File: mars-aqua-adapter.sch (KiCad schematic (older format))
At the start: 40 parts, among them J1 Conn_01x03, J2 Conn_01x03, J3 Conn_01x04, J4 Conn_01x04, J5 Conn_01x03, J6 Conn_01x03, Q2 Q_PNP_BEC, U1 LM358, U2 LM393

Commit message: Final Layout
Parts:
- C1, C4: footprint Capacitor_SMD:C_1206_3216Metric_Pad1.42x1.75mm_HandSolder -> Capacitor_SMD:C_0805_2012Metric
- C2, C3: value 0.1uF -> 4.7uF; footprint Capacitor_SMD:C_1206_3216Metric_Pad1.42x1.75mm_HandSolder -> Capacitor_SMD:C_0805_2012Metric
- gave numbers to parts that had none: 1
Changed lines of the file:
@@
 P 3500 2850
 F 0 "C2" H 3592 2896 50  0000 L CNN
-F 1 "0.1uF" H 3592 2805 50  0000 L CNN
-F 2 "Capacitor_SMD:C_1206_3216Metric_Pad1.42x1.75mm_HandSolder" H 3500 2850 50  0001 C CNN
+F 1 "4.7uF" H 3592 2805 50  0000 L CNN
+F 2 "Capacitor_SMD:C_0805_2012Metric" H 3500 2850 50  0001 C CNN
 F 3 "~" H 3500 2850 50  0001 C CNN
 	1    3500 2850
@@
 F 0 "C4" H 6942 1246 50  0000 L CNN
 F 1 "0.1uF" H 6942 1155 50  0000 L CNN
-F 2 "Capacitor_SMD:C_1206_3216Metric_Pad1.42x1.75mm_HandSolder" H 6850 1200 50  0001 C CNN
+F 2 "Capacitor_SMD:C_0805_2012Metric" H 6850 1200 50  0001 C CNN
 F 3 "~" H 6850 1200 50  0001 C CNN
 	1    6850 1200
@@
 F 0 "C1" H 3792 1646 50  0000 L CNN
 F 1 "0.1uF" H 3792 1555 50  0000 L CNN
-F 2 "Capacitor_SMD:C_1206_3216Metric_Pad1.42x1.75mm_HandSolder" H 3700 1600 50  0001 C CNN
+F 2 "Capacitor_SMD:C_0805_2012Metric" H 3700 1600 50  0001 C CNN
 F 3 "~" H 3700 1600 50  0001 C CNN
 	1    3700 1600
@@
 P 3500 5150
 F 0 "C3" H 3592 5196 50  0000 L CNN
-F 1 "0.1uF" H 3592 5105 50  0000 L CNN
-F 2 "Capacitor_SMD:C_1206_3216Metric_Pad1.42x1.75mm_HandSolder" H 3500 5150 50  0001 C CNN
+F 1 "4.7uF" H 3592 5105 50  0000 L CNN
+F 2 "Capacitor_SMD:C_0805_2012Metric" H 3500 5150 50  0001 C CNN
 F 3 "~" H 3500 5150 50  0001 C CNN
 	1    3500 5150
@@
 $EndComp
 $Comp
-L Device:Q_PNP_BEC Q?
+L Device:Q_PNP_BEC Q1
 U 1 1 5C86EAA4
 P 8200 2600
-F 0 "Q?" H 8391 2554 50  0000 L CNN
+F 0 "Q1" H 8391 2554 50  0000 L CNN
 F 1 "Q_PNP_BEC" H 8391 2645 50  0000 L CNN
 F 2 "Package_TO_SOT_SMD:SOT-23" H 8400 2700 50  0001 C CNN

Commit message: Fix traces on comparator
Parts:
- R11, R13: value 30k -> 39k
- R12, R14: value 10k -> 20k
- VR1, VR2: value TRIMPOT-SMD-3MM-OPEN-1_10W-25% -> 10k
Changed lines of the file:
@@
 P 6000 2750
 F 0 "R12" H 6068 2796 50  0000 L CNN
-F 1 "10k" H 6068 2705 50  0000 L CNN
+F 1 "20k" H 6068 2705 50  0000 L CNN
 F 2 "Resistor_SMD:R_0603_1608Metric_Pad1.05x0.95mm_HandSolder" V 6040 2740 50  0001 C CNN
 F 3 "~" H 6000 2750 50  0001 C CNN
@@
 P 6000 2350
 F 0 "R11" H 6068 2396 50  0000 L CNN
-F 1 "30k" H 6068 2305 50  0000 L CNN
+F 1 "39k" H 6068 2305 50  0000 L CNN
 F 2 "Resistor_SMD:R_0603_1608Metric_Pad1.05x0.95mm_HandSolder" V 6040 2340 50  0001 C CNN
 F 3 "~" H 6000 2350 50  0001 C CNN
@@
 P 6000 1900
 F 0 "VR1" H 5933 1805 45  0000 R CNN
-F 1 "TRIMPOT-SMD-3MM-OPEN-1_10W-25%" H 5933 1889 45  0000 R CNN
+F 1 "10k" H 5933 1889 45  0000 R CNN
 F 2 "Resistors:TRIMPOT-SMD-3MM-OPEN" V 5850 1900 20  0001 C CNN
 F 3 "" H 6000 1900 60  0001 C CNN
@@
 P 6000 5050
 F 0 "R14" H 6068 5096 50  0000 L CNN
-F 1 "10k" H 6068 5005 50  0000 L CNN
+F 1 "20k" H 6068 5005 50  0000 L CNN
 F 2 "Resistor_SMD:R_0603_1608Metric_Pad1.05x0.95mm_HandSolder" V 6040 5040 50  0001 C CNN
 F 3 "~" H 6000 5050 50  0001 C CNN
@@
 P 6000 4650
 F 0 "R13" H 6068 4696 50  0000 L CNN
-F 1 "30k" H 6068 4605 50  0000 L CNN
+F 1 "39k" H 6068 4605 50  0000 L CNN
 F 2 "Resistor_SMD:R_0603_1608Metric_Pad1.05x0.95mm_HandSolder" V 6040 4640 50  0001 C CNN
 F 3 "~" H 6000 4650 50  0001 C CNN
@@
 P 6000 4200
 F 0 "VR2" H 5933 4105 45  0000 R CNN
-F 1 "TRIMPOT-SMD-3MM-OPEN-1_10W-25%" H 5933 4189 45  0000 R CNN
+F 1 "10k" H 5933 4189 45  0000 R CNN
 F 2 "Resistors:TRIMPOT-SMD-3MM-OPEN" V 5850 4200 20  0001 C CNN
 F 3 "" H 6000 4200 60  0001 C CNN

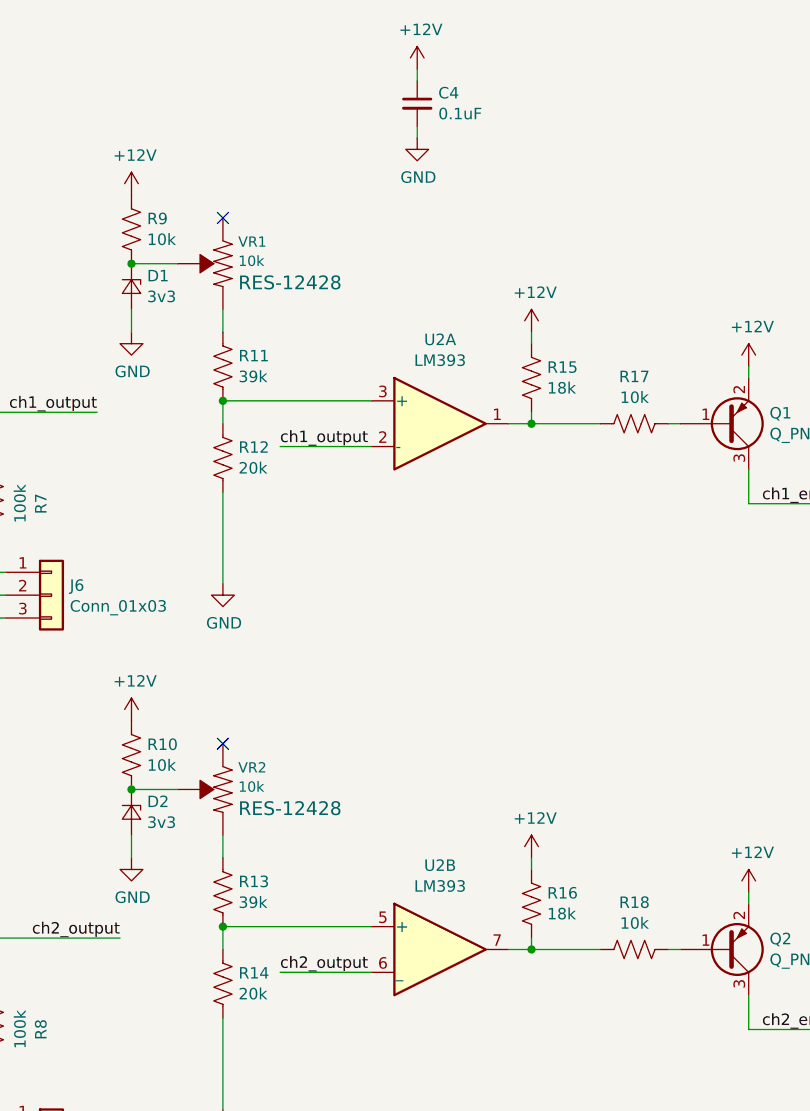
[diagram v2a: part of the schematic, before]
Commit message: Add hysteresis
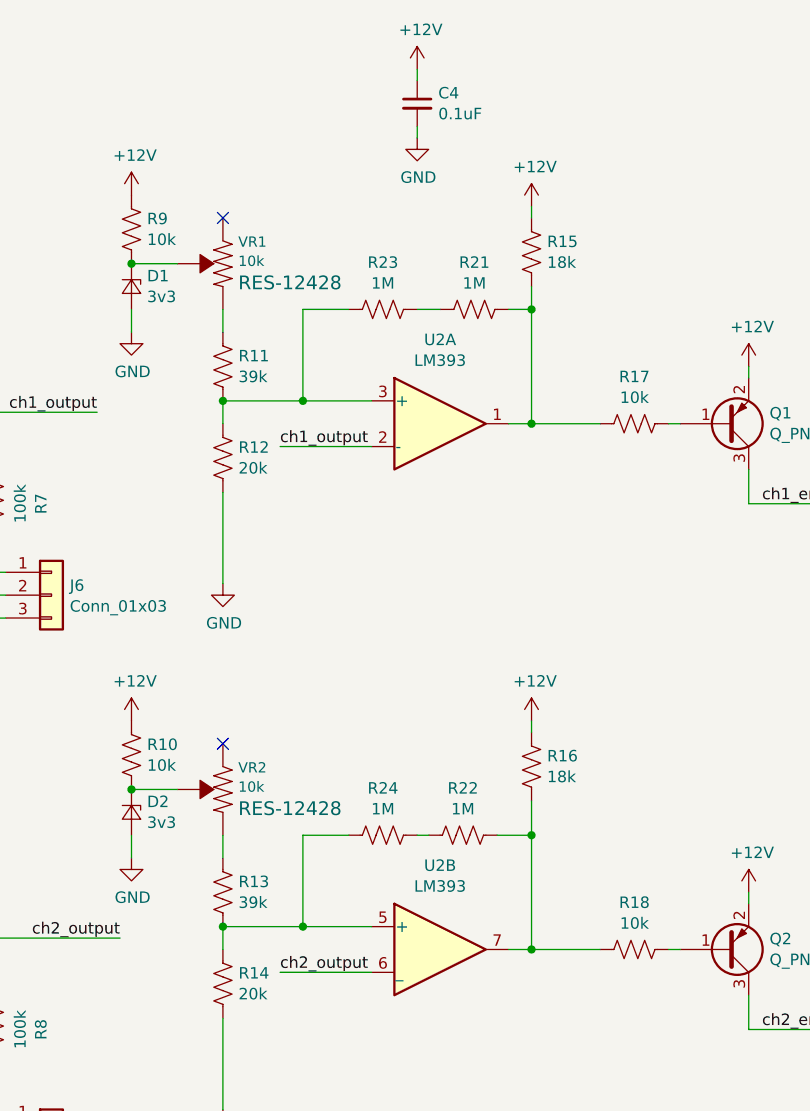
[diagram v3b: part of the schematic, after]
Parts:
- added R21, R22, R23, R24: 1M, Resistor_SMD:R_0603_1608Metric_Pad1.05x0.95mm_HandSolder, symbol Device:R_US
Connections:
- net at R15.2, R17.2, U2.1: now also R21.1
- net at R11.2, R12.1, U2.3 (+): now also R23.2
- net at R13.2, R14.1, U2.5 (+): now also R24.2
- net at R16.2, R18.2, U2.7: now also R22.1
- new net: R22.2, R24.1
- new net: R21.2, R23.1
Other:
- moved on the sheet: R15, R16
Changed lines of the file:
@@
 L Device:R_US R15
 U 1 1 5C8039BD
-P 7350 2400
-F 0 "R15" H 7418 2446 50  0000 L CNN
-F 1 "18k" H 7418 2355 50  0000 L CNN
-F 2 "Resistor_SMD:R_0603_1608Metric_Pad1.05x0.95mm_HandSolder" V 7390 2390 50  0001 C CNN
-F 3 "~" H 7350 2400 50  0001 C CNN
-	1    7350 2400
+P 7350 1850
+F 0 "R15" H 7418 1896 50  0000 L CNN
+F 1 "18k" H 7418 1805 50  0000 L CNN
+F 2 "Resistor_SMD:R_0603_1608Metric_Pad1.05x0.95mm_HandSolder" V 7390 1840 50  0001 C CNN
+F 3 "~" H 7350 1850 50  0001 C CNN
+	1    7350 1850
 	1    0    0    -1
 $EndComp
@@
 $EndComp
 Wire Wire Line
-	6000 2500 6650 2500
+	6000 2500 6350 2500
 Wire Wire Line
 	6000 2500 6000 2600
@@
 L power:+12V #PWR017
 U 1 1 5C80C6D6
-P 7350 2200
-F 0 "#PWR017" H 7350 2050 50  0001 C CNN
-F 1 "+12V" H 7365 2373 50  0000 C CNN
-F 2 "" H 7350 2200 50  0001 C CNN
-F 3 "" H 7350 2200 50  0001 C CNN
-	1    7350 2200
+P 7350 1650
+F 0 "#PWR017" H 7350 1500 50  0001 C CNN
+F 1 "+12V" H 7365 1823 50  0000 C CNN
+F 2 "" H 7350 1650 50  0001 C CNN
+F 3 "" H 7350 1650 50  0001 C CNN
+	1    7350 1650
 	1    0    0    -1
 $EndComp
@@
 	7250 2600 7350 2600
 Wire Wire Line
-	7350 2600 7350 2550
-Wire Wire Line
-	7350 2250 7350 2200
+	7350 1700 7350 1650
 Wire Wire Line
 	7650 2600 7350 2600
@@
 L Device:R_US R16
 U 1 1 5C84869D
-P 7350 4700
-F 0 "R16" H 7418 4746 50  0000 L CNN
-F 1 "18k" H 7418 4655 50  0000 L CNN
-F 2 "Resistor_SMD:R_0603_1608Metric_Pad1.05x0.95mm_HandSolder" V 7390 4690 50  0001 C CNN
-F 3 "~" H 7350 4700 50  0001 C CNN
-	1    7350 4700
+P 7350 4100
+F 0 "R16" H 7418 4146 50  0000 L CNN
+F 1 "18k" H 7418 4055 50  0000 L CNN
+F 2 "Resistor_SMD:R_0603_1608Metric_Pad1.05x0.95mm_HandSolder" V 7390 4090 50  0001 C CNN
+F 3 "~" H 7350 4100 50  0001 C CNN
+	1    7350 4100
 	1    0    0    -1
 $EndComp
@@
 $EndComp
 Wire Wire Line
-	6000 4800 6650 4800
+	6000 4800 6350 4800
 Wire Wire Line
 	6000 4800 6000 4900
@@
 L power:+12V #PWR018
 U 1 1 5C8486D0
-P 7350 4500
-F 0 "#PWR018" H 7350 4350 50  0001 C CNN
-F 1 "+12V" H 7365 4673 50  0000 C CNN
-F 2 "" H 7350 4500 50  0001 C CNN
-F 3 "" H 7350 4500 50  0001 C CNN
-	1    7350 4500
+P 7350 3900
+F 0 "#PWR018" H 7350 3750 50  0001 C CNN
+F 1 "+12V" H 7365 4073 50  0000 C CNN
+F 2 "" H 7350 3900 50  0001 C CNN
+F 3 "" H 7350 3900 50  0001 C CNN
+	1    7350 3900
 	1    0    0    -1
 $EndComp
@@
 	7250 4900 7350 4900
 Wire Wire Line
-	7350 4900 7350 4850
-Wire Wire Line
-	7350 4550 7350 4500
+	7350 3950 7350 3900
 Wire Wire Line
 	7650 4900 7350 4900
@@
 	1    0    0    1
 $EndComp
+$Comp
+L Device:R_US R22
+U 1 1 5CEC30DE
+P 7050 4400
+F 0 "R22" V 6845 4400 50  0000 C CNN
+F 1 "1M" V 6936 4400 50  0000 C CNN
+F 2 "Resistor_SMD:R_0603_1608Metric_Pad1.05x0.95mm_HandSolder" V 7090 4390 50  0001 C CNN
+F 3 "~" H 7050 4400 50  0001 C CNN
+	1    7050 4400
+	0    1    1    0
+$EndComp
+Wire Wire Line
+	6350 4400 6350 4800
+Connection ~ 6350 4800
+Wire Wire Line
+	6350 4800 6650 4800
+$Comp
+L Device:R_US R21
+U 1 1 5CECEA87
+P 7100 2100
+F 0 "R21" V 6895 2100 50  0000 C CNN
+F 1 "1M" V 6986 2100 50  0000 C CNN
+F 2 "Resistor_SMD:R_0603_1608Metric_Pad1.05x0.95mm_HandSolder" V 7140 2090 50  0001 C CNN
+F 3 "~" H 7100 2100 50  0001 C CNN
+	1    7100 2100
+	0    1    1    0
+$EndComp
+Wire Wire Line
+	6350 2100 6350 2500
+Connection ~ 6350 2500
+Wire Wire Line
+	6350 2500 6650 2500
+Wire Wire Line
+	7350 2000 7350 2100
+$Comp
+L Device:R_US R23
+U 1 1 5CEDC5E4
+P 6700 2100
+F 0 "R23" V 6495 2100 50  0000 C CNN
+F 1 "1M" V 6586 2100 50  0000 C CNN
+F 2 "Resistor_SMD:R_0603_1608Metric_Pad1.05x0.95mm_HandSolder" V 6740 2090 50  0001 C CNN
+F 3 "~" H 6700 2100 50  0001 C CNN
+	1    6700 2100
+	0    1    1    0
+$EndComp
+Wire Wire Line
+	6350 2100 6550 2100
+Wire Wire Line
+	6850 2100 6950 2100
+Wire Wire Line
+	7250 2100 7350 2100
+Connection ~ 7350 2100
+Wire Wire Line
+	7350 2100 7350 2600
+Wire Wire Line
+	7350 4250 7350 4400
+$Comp
+L Device:R_US R24
+U 1 1 5CEE68E2
+P 6700 4400
+F 0 "R24" V 6495 4400 50  0000 C CNN
+F 1 "1M" V 6586 4400 50  0000 C CNN
+F 2 "Resistor_SMD:R_0603_1608Metric_Pad1.05x0.95mm_HandSolder" V 6740 4390 50  0001 C CNN
+F 3 "~" H 6700 4400 50  0001 C CNN
+	1    6700 4400
+	0    1    1    0
+$EndComp
+Wire Wire Line
+	6350 4400 6550 4400
+Wire Wire Line
+	6850 4400 6900 4400
+Wire Wire Line
+	7200 4400 7350 4400
+Connection ~ 7350 4400
+Wire Wire Line
+	7350 4400 7350 4900
 $EndSCHEMATC
